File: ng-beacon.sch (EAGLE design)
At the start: 2 parts

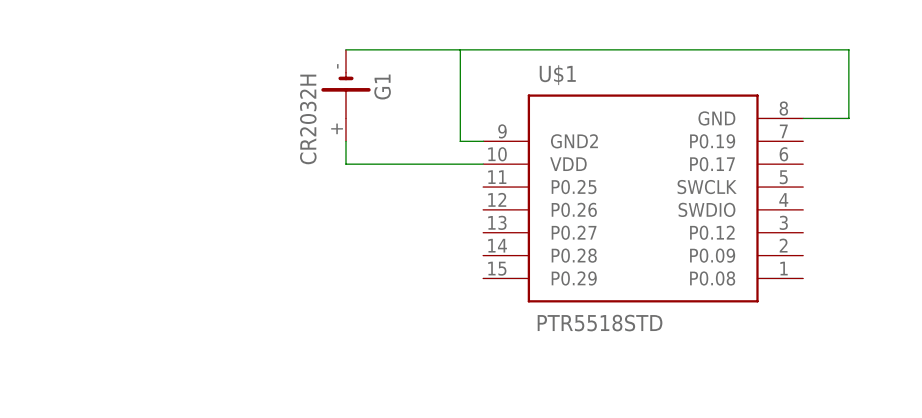
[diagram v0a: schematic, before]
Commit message: add switch
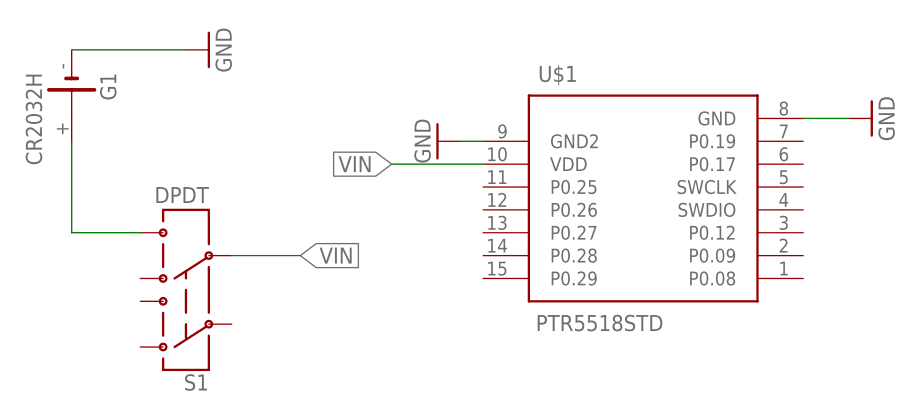
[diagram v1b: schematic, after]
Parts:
- added S1: DPDT, SparkFun-Electromechanical:SWITCH-DPDTAYZ0202
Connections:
- net N$2 renamed GND
- new net VIN: S1.5, U$1.VDD
- net N$1: now also S1.6; no longer U$1.VDD
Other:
- moved on the sheet: G1

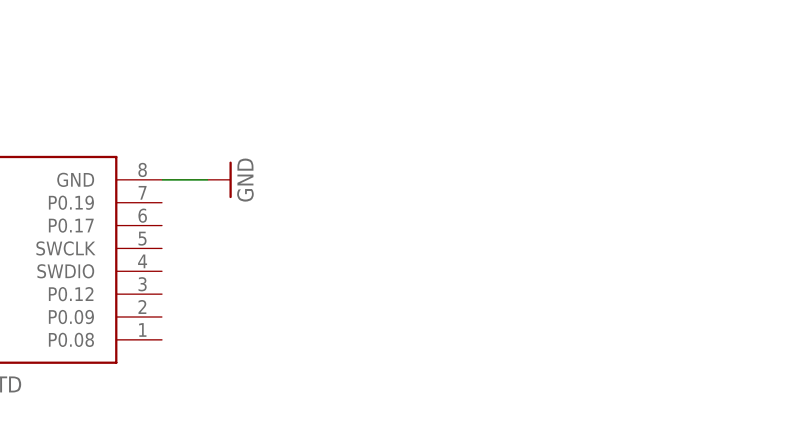
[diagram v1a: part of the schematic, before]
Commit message: add programming port
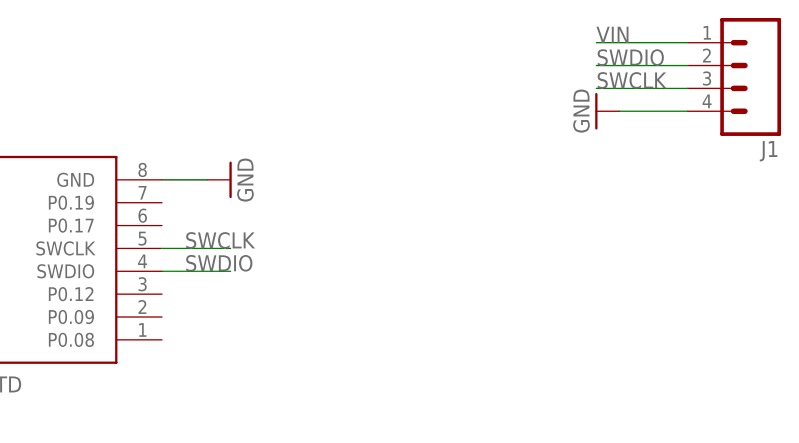
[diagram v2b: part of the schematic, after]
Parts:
- added J1: (no value), SparkFun-Connectors:M04LOCK
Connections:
- new net SWCLK: J1.3, U$1.SWCLK
- new net SWDIO: J1.2, U$1.SWDIO
- net GND: now also J1.4
- net VIN: now also J1.1
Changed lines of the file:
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@@
 <layer number="112" name="tSilk" color="7" fill="1" visible="yes" active="yes"/>
 <layer number="113" name="IDFDebug" color="4" fill="1" visible="yes" active="yes"/>
+<layer number="114" name="Badge_Outline" color="7" fill="1" visible="yes" active="yes"/>
+<layer number="115" name="ReferenceISLANDS" color="7" fill="1" visible="yes" active="yes"/>
 <layer number="116" name="Patch_BOT" color="9" fill="4" visible="yes" active="yes"/>
 <layer number="118" name="Rect_Pads" color="7" fill="1" visible="yes" active="yes"/>
@@
 <part name="GND2" library="SparkFun-Aesthetics" deviceset="GND" device=""/>
 <part name="GND3" library="SparkFun-Aesthetics" deviceset="GND" device=""/>
+<part name="J1" library="SparkFun-Connectors" deviceset="M04" device="LOCK"/>
+<part name="GND8" library="SparkFun-Aesthetics" deviceset="GND" device=""/>
 </parts>
 <sheets>
@@
 <instance part="GND2" gate="1" x="55.88" y="68.58" rot="R90"/>
 <instance part="GND3" gate="1" x="7.62" y="66.04" rot="R270"/>
+<instance part="J1" gate="G$1" x="111.76" y="81.28" rot="R180"/>
+<instance part="GND8" gate="1" x="96.52" y="76.2" rot="R270"/>
 </instances>
 <busses>
@@
 <wire x1="10.16" y1="66.04" x2="12.7" y2="66.04" width="0.1524" layer="91"/>
 <pinref part="GND3" gate="1" pin="GND"/>
+</segment>
+<segment>
+<pinref part="GND8" gate="1" pin="GND"/>
+<pinref part="J1" gate="G$1" pin="4"/>
+<wire x1="99.06" y1="76.2" x2="106.68" y2="76.2" width="0.1524" layer="91"/>
 </segment>
 </net>
@@
 <label x="2.54" y="63.5" size="1.778" layer="95" rot="R180" xref="yes"/>
 </segment>
+<segment>
+<pinref part="J1" gate="G$1" pin="1"/>
+<wire x1="106.68" y1="83.82" x2="96.52" y2="83.82" width="0.1524" layer="91"/>
+<label x="96.52" y="83.82" size="1.778" layer="95"/>
+</segment>
 </net>
+<net name="SWCLK" class="0">
+<segment>
+<pinref part="J1" gate="G$1" pin="3"/>
+<wire x1="106.68" y1="78.74" x2="96.52" y2="78.74" width="0.1524" layer="91"/>
+<label x="96.52" y="78.74" size="1.778" layer="95"/>
+</segment>
+<segment>
+<pinref part="U$1" gate="G$1" pin="SWCLK"/>
+<wire x1="48.26" y1="60.96" x2="55.88" y2="60.96" width="0.1524" layer="91"/>
+<label x="50.8" y="60.96" size="1.778" layer="95"/>
+</segment>
+</net>
+<net name="SWDIO" class="0">
+<segment>
+<pinref part="J1" gate="G$1" pin="2"/>
+<wire x1="106.68" y1="81.28" x2="96.52" y2="81.28" width="0.1524" layer="91"/>
+<label x="96.52" y="81.28" size="1.778" layer="95"/>
+</segment>
+<segment>
+<pinref part="U$1" gate="G$1" pin="SWDIO"/>
+<wire x1="48.26" y1="58.42" x2="55.88" y2="58.42" width="0.1524" layer="91"/>
+<label x="50.8" y="58.42" size="1.778" layer="95"/>
+</segment>
+</net>

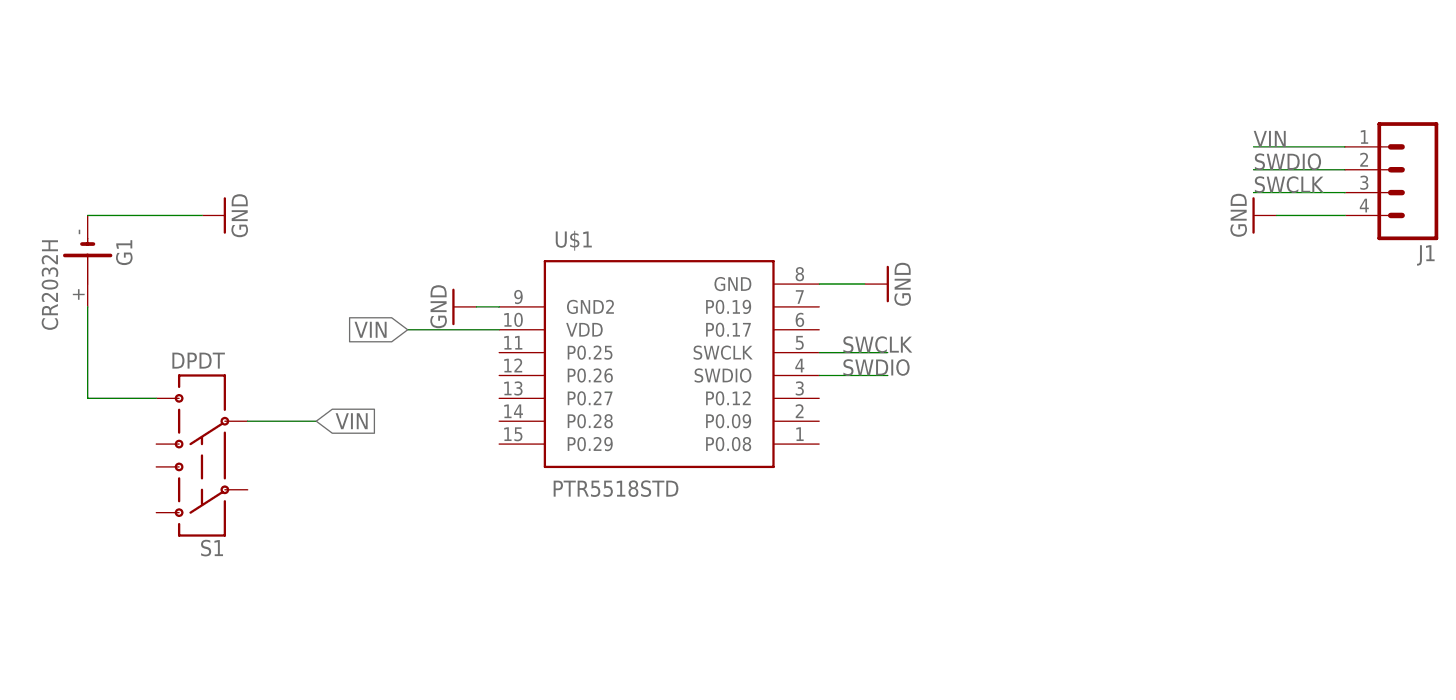
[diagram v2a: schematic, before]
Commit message: add temperature sensor
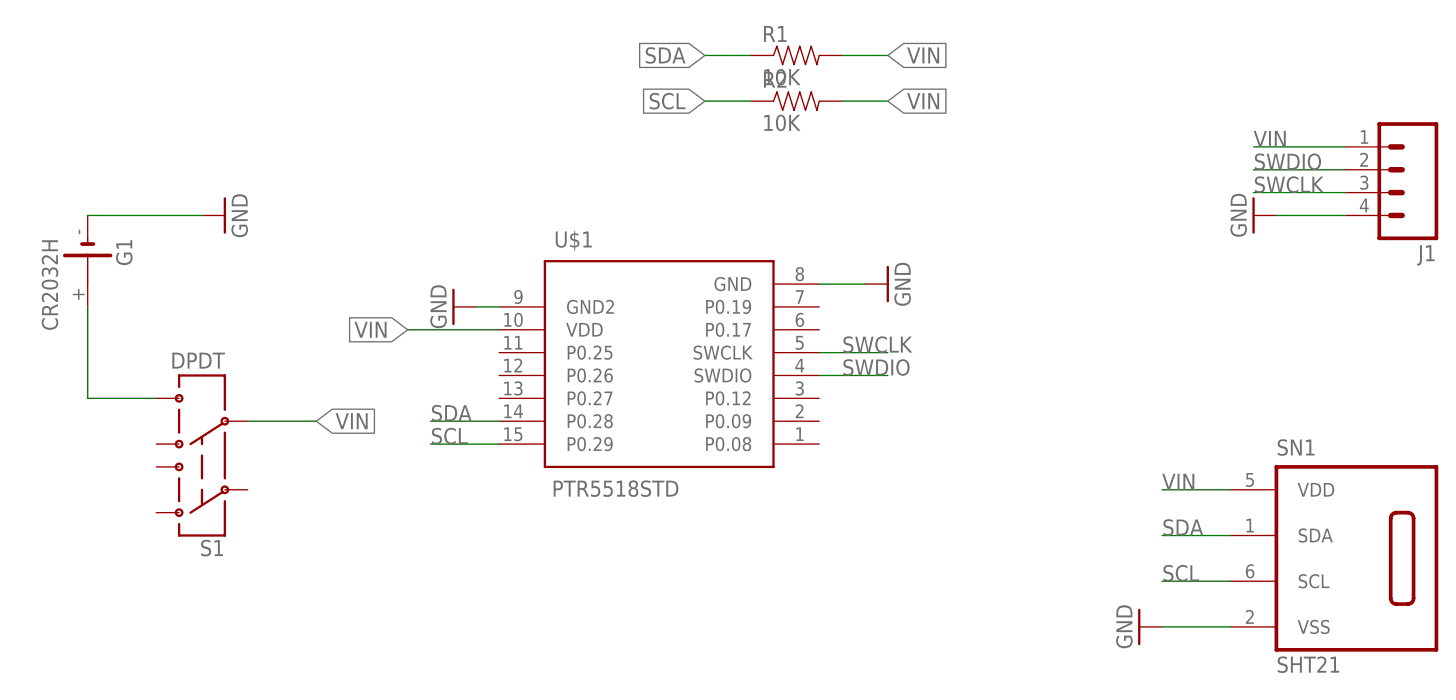
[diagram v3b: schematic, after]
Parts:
- added R1, R2: 10K, SparkFun-Resistors:10KOHM-1/10W-1%(0603)0603
- added SN1: SHT21, sensirion:SHT21
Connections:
- new net SCL: R2.1, SN1.SCL, U$1.P0.29
- new net SDA: R1.1, SN1.SDA, U$1.P0.28
- net GND: now also SN1.VSS
- net VIN: now also R1.2, R2.2, SN1.VDD
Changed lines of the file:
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@@
 <part name="J1" library="SparkFun-Connectors" deviceset="M04" device="LOCK"/>
 <part name="GND8" library="SparkFun-Aesthetics" deviceset="GND" device=""/>
+<part name="SN1" library="sensirion" deviceset="SHT21" device=""/>
+<part name="GND4" library="SparkFun-Aesthetics" deviceset="GND" device=""/>
+<part name="R1" library="SparkFun-Resistors" deviceset="10KOHM-1/10W-1%(0603)" device="0603" value="10K"/>
+<part name="R2" library="SparkFun-Resistors" deviceset="10KOHM-1/10W-1%(0603)" device="0603" value="10K"/>
 </parts>
 <sheets>
@@
 <instance part="J1" gate="G$1" x="111.76" y="81.28" rot="R180"/>
 <instance part="GND8" gate="1" x="96.52" y="76.2" rot="R270"/>
+<instance part="SN1" gate="G$1" x="106.68" y="38.1"/>
+<instance part="GND4" gate="1" x="83.82" y="30.48" rot="R270"/>
+<instance part="R1" gate="G$1" x="45.72" y="93.98"/>
+<instance part="R2" gate="G$1" x="45.72" y="88.9"/>
 </instances>
 <busses>
@@
 <pinref part="J1" gate="G$1" pin="4"/>
 <wire x1="99.06" y1="76.2" x2="106.68" y2="76.2" width="0.1524" layer="91"/>
+</segment>
+<segment>
+<pinref part="SN1" gate="G$1" pin="VSS"/>
+<wire x1="93.98" y1="30.48" x2="86.36" y2="30.48" width="0.1524" layer="91"/>
+<pinref part="GND4" gate="1" pin="GND"/>
 </segment>
 </net>
@@
 <label x="96.52" y="83.82" size="1.778" layer="95"/>
 </segment>
+<segment>
+<pinref part="SN1" gate="G$1" pin="VDD"/>
+<wire x1="93.98" y1="45.72" x2="86.36" y2="45.72" width="0.1524" layer="91"/>
+<label x="86.36" y="45.72" size="1.778" layer="95"/>
+</segment>
+<segment>
+<pinref part="R1" gate="G$1" pin="2"/>
+<wire x1="50.8" y1="93.98" x2="55.88" y2="93.98" width="0.1524" layer="91"/>
+<label x="55.88" y="93.98" size="1.778" layer="95" xref="yes"/>
+</segment>
+<segment>
+<pinref part="R2" gate="G$1" pin="2"/>
+<wire x1="50.8" y1="88.9" x2="55.88" y2="88.9" width="0.1524" layer="91"/>
+<label x="55.88" y="88.9" size="1.778" layer="95" xref="yes"/>
+</segment>
 </net>
 <net name="SWCLK" class="0">
@@
 </segment>
 </net>
+<net name="SDA" class="0">
+<segment>
+<pinref part="U$1" gate="G$1" pin="P0.28"/>
+<wire x1="12.7" y1="53.34" x2="5.08" y2="53.34" width="0.1524" layer="91"/>
+<label x="5.08" y="53.34" size="1.778" layer="95"/>
+</segment>
+<segment>
+<pinref part="SN1" gate="G$1" pin="SDA"/>
+<wire x1="93.98" y1="40.64" x2="86.36" y2="40.64" width="0.1524" layer="91"/>
+<label x="86.36" y="40.64" size="1.778" layer="95"/>
+</segment>
+<segment>
+<pinref part="R1" gate="G$1" pin="1"/>
+<wire x1="35.56" y1="93.98" x2="40.64" y2="93.98" width="0.1524" layer="91"/>
+<label x="35.56" y="93.98" size="1.778" layer="95" rot="R180" xref="yes"/>
+</segment>
+</net>
+<net name="SCL" class="0">
+<segment>
+<pinref part="U$1" gate="G$1" pin="P0.29"/>
+<wire x1="12.7" y1="50.8" x2="5.08" y2="50.8" width="0.1524" layer="91"/>
+<label x="5.08" y="50.8" size="1.778" layer="95"/>
+</segment>
+<segment>
+<pinref part="SN1" gate="G$1" pin="SCL"/>
+<wire x1="93.98" y1="35.56" x2="86.36" y2="35.56" width="0.1524" layer="91"/>
+<label x="86.36" y="35.56" size="1.778" layer="95"/>
+</segment>
+<segment>
+<pinref part="R2" gate="G$1" pin="1"/>
+<wire x1="40.64" y1="88.9" x2="35.56" y2="88.9" width="0.1524" layer="91"/>
+<label x="35.56" y="88.9" size="1.778" layer="95" rot="R180" xref="yes"/>
+</segment>
+</net>

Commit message: replace battery connector
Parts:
- G1: value CR2032H -> 20mm coincell; device battery:CR2032H -> SparkFun-Electromechanical:BATTERY20MM_4LEGS
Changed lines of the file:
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@@
 <parts>
 <part name="U$1" library="PTR5518" deviceset="PTR5518" device="STD"/>
-<part name="G1" library="battery" deviceset="CR2032H" device=""/>
+<part name="G1" library="SparkFun-Electromechanical" deviceset="BATTERY" device="20MM_4LEGS" value="20mm coincell"/>
 <part name="S1" library="SparkFun-Electromechanical" deviceset="SWITCH-DPDT" device="AYZ0202" value="DPDT"/>
 <part name="GND1" library="SparkFun-Aesthetics" deviceset="GND" device=""/>
@@
 <instances>
 <instance part="U$1" gate="G$1" x="30.48" y="58.42"/>
-<instance part="G1" gate="1" x="-33.02" y="71.12" rot="R270"/>
+<instance part="G1" gate="G$1" x="-33.02" y="71.12" rot="R90"/>
 <instance part="S1" gate="G$1" x="-20.32" y="48.26" rot="R180"/>
 <instance part="GND1" gate="1" x="-17.78" y="76.2" rot="R90"/>
@@
 <segment>
 <pinref part="GND1" gate="1" pin="GND"/>
-<pinref part="G1" gate="1" pin="-"/>
+<pinref part="G1" gate="G$1" pin="-"/>
 <wire x1="-33.02" y1="76.2" x2="-20.32" y2="76.2" width="0.1524" layer="91"/>
 </segment>
@@
 <net name="N$1" class="0">
 <segment>
-<pinref part="G1" gate="1" pin="+"/>
+<pinref part="G1" gate="G$1" pin="+"/>
 <wire x1="-33.02" y1="66.04" x2="-33.02" y2="55.88" width="0.1524" layer="91"/>
 <pinref part="S1" gate="G$1" pin="6"/>
